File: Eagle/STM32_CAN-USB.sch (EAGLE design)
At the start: 51 parts, among them IC1 STM32F105RBT, IC2 TJA1055T, IC3 BD9G101G, IC4 LM1117IMPX-3.3, Q1 16MHz, X1 MINI-USB

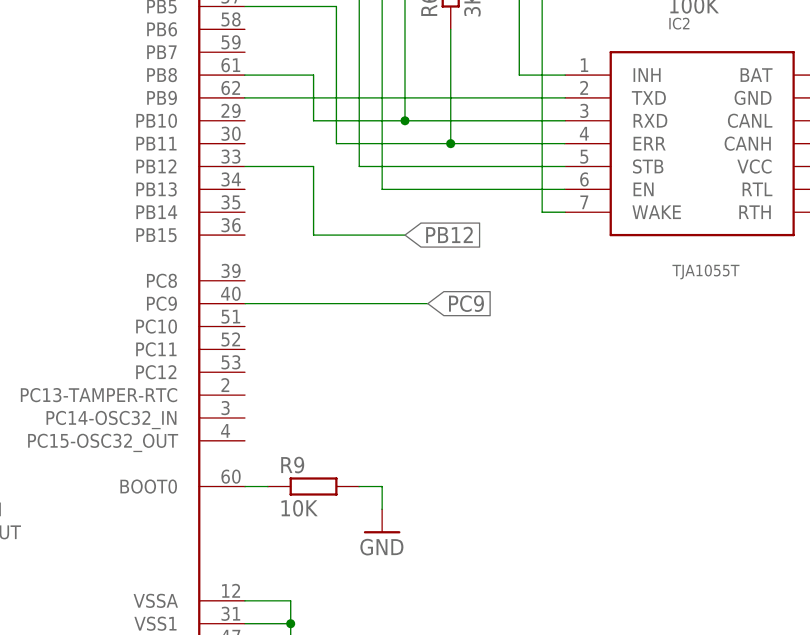
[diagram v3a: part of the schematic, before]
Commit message: added pull-down resistors on the lines EN and STB
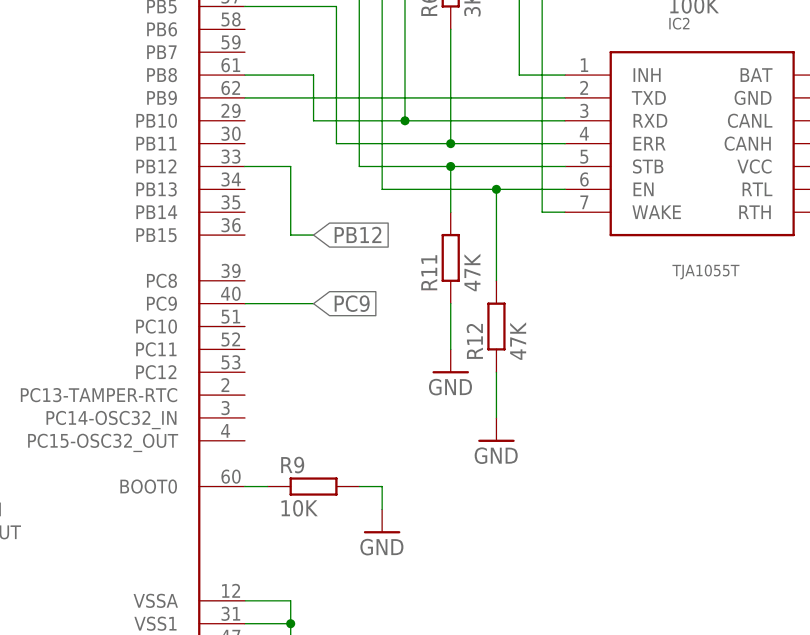
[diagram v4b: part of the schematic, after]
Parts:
- added R11, R12: 47K, rcl:R-EU_R0805
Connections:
- net GND: now also R11.1, R12.1
- net N$14: now also R12.2
- net N$6: now also R11.2
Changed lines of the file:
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@@
 <?xml version="1.0" encoding="utf-8"?>
 <!DOCTYPE eagle SYSTEM "eagle.dtd">
-<eagle version="7.4.0">
+<eagle version="7.2.0">
 <drawing>
 <settings>
@@
 <part name="GND18" library="supply1" deviceset="GND" device=""/>
 <part name="GPIO" library="pinhead" deviceset="PINHD-1X4" device=""/>
+<part name="R11" library="rcl" deviceset="R-EU_" device="R0805" value="47K"/>
+<part name="R12" library="rcl" deviceset="R-EU_" device="R0805" value="47K"/>
+<part name="GND19" library="supply1" deviceset="GND" device=""/>
+<part name="GND20" library="supply1" deviceset="GND" device=""/>
 </parts>
 <sheets>
@@
 <instance part="GND18" gate="1" x="-40.64" y="-45.72"/>
 <instance part="GPIO" gate="A" x="2.54" y="-33.02"/>
+<instance part="R11" gate="G$1" x="111.76" y="50.8" rot="R90"/>
+<instance part="R12" gate="G$1" x="116.84" y="43.18" rot="R90"/>
+<instance part="GND19" gate="1" x="111.76" y="38.1"/>
+<instance part="GND20" gate="1" x="116.84" y="30.48"/>
 </instances>
 <busses>
@@
 <pinref part="GPIO" gate="A" pin="1"/>
 <wire x1="0" y1="-27.94" x2="-40.64" y2="-27.94" width="0.1524" layer="91"/>
+</segment>
+<segment>
+<pinref part="R11" gate="G$1" pin="1"/>
+<pinref part="GND19" gate="1" pin="GND"/>
+<wire x1="111.76" y1="45.72" x2="111.76" y2="40.64" width="0.1524" layer="91"/>
+</segment>
+<segment>
+<pinref part="R12" gate="G$1" pin="1"/>
+<pinref part="GND20" gate="1" pin="GND"/>
+<wire x1="116.84" y1="38.1" x2="116.84" y2="33.02" width="0.1524" layer="91"/>
 </segment>
 </net>
@@
 <segment>
 <pinref part="IC2" gate="G$1" pin="EN"/>
-<wire x1="124.46" y1="58.42" x2="104.14" y2="58.42" width="0.1524" layer="91"/>
+<wire x1="124.46" y1="58.42" x2="116.84" y2="58.42" width="0.1524" layer="91"/>
+<wire x1="116.84" y1="58.42" x2="104.14" y2="58.42" width="0.1524" layer="91"/>
 <wire x1="104.14" y1="58.42" x2="104.14" y2="83.82" width="0.1524" layer="91"/>
 <pinref part="IC1" gate="MCU" pin="PB3"/>
 <wire x1="88.9" y1="83.82" x2="104.14" y2="83.82" width="0.1524" layer="91"/>
+<pinref part="R12" gate="G$1" pin="2"/>
+<wire x1="116.84" y1="48.26" x2="116.84" y2="58.42" width="0.1524" layer="91"/>
+<junction x="116.84" y="58.42"/>
 </segment>
 </net>
@@
 <segment>
 <pinref part="IC2" gate="G$1" pin="STB"/>
-<wire x1="124.46" y1="60.96" x2="101.6" y2="60.96" width="0.1524" layer="91"/>
+<wire x1="124.46" y1="60.96" x2="111.76" y2="60.96" width="0.1524" layer="91"/>
+<wire x1="111.76" y1="60.96" x2="101.6" y2="60.96" width="0.1524" layer="91"/>
 <wire x1="101.6" y1="60.96" x2="101.6" y2="81.28" width="0.1524" layer="91"/>
 <pinref part="IC1" gate="MCU" pin="PB4"/>
 <wire x1="88.9" y1="81.28" x2="101.6" y2="81.28" width="0.1524" layer="91"/>
+<pinref part="R11" gate="G$1" pin="2"/>
+<wire x1="111.76" y1="55.88" x2="111.76" y2="60.96" width="0.1524" layer="91"/>
+<junction x="111.76" y="60.96"/>
 </segment>
 </net>
@@
 <segment>
 <pinref part="IC1" gate="MCU" pin="PC9"/>
-<wire x1="88.9" y1="45.72" x2="109.22" y2="45.72" width="0.1524" layer="91"/>
-<label x="109.22" y="45.72" size="1.778" layer="95" xref="yes"/>
+<wire x1="88.9" y1="45.72" x2="96.52" y2="45.72" width="0.1524" layer="91"/>
+<label x="96.52" y="45.72" size="1.778" layer="95" xref="yes"/>
 </segment>
 <segment>
@@
 <segment>
 <pinref part="IC1" gate="MCU" pin="PB12"/>
-<wire x1="88.9" y1="60.96" x2="96.52" y2="60.96" width="0.1524" layer="91"/>
-<wire x1="96.52" y1="60.96" x2="96.52" y2="53.34" width="0.1524" layer="91"/>
-<wire x1="96.52" y1="53.34" x2="106.68" y2="53.34" width="0.1524" layer="91"/>
-<label x="106.68" y="53.34" size="1.778" layer="95" xref="yes"/>
-</segment>
-<segment>
+<wire x1="88.9" y1="60.96" x2="93.98" y2="60.96" width="0.1524" layer="91"/>
+<wire x1="93.98" y1="60.96" x2="93.98" y2="53.34" width="0.1524" layer="91"/>
+<wire x1="93.98" y1="53.34" x2="96.52" y2="53.34" width="0.1524" layer="91"/>
+<label x="96.52" y="53.34" size="1.778" layer="95" xref="yes"/>
+</segment>
+<segment>
